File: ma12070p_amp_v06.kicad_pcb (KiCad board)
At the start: 2 copper layers, 100.4 x 80.4 mm, 83 parts, among them U1 MAX16956, U2 MA12070P

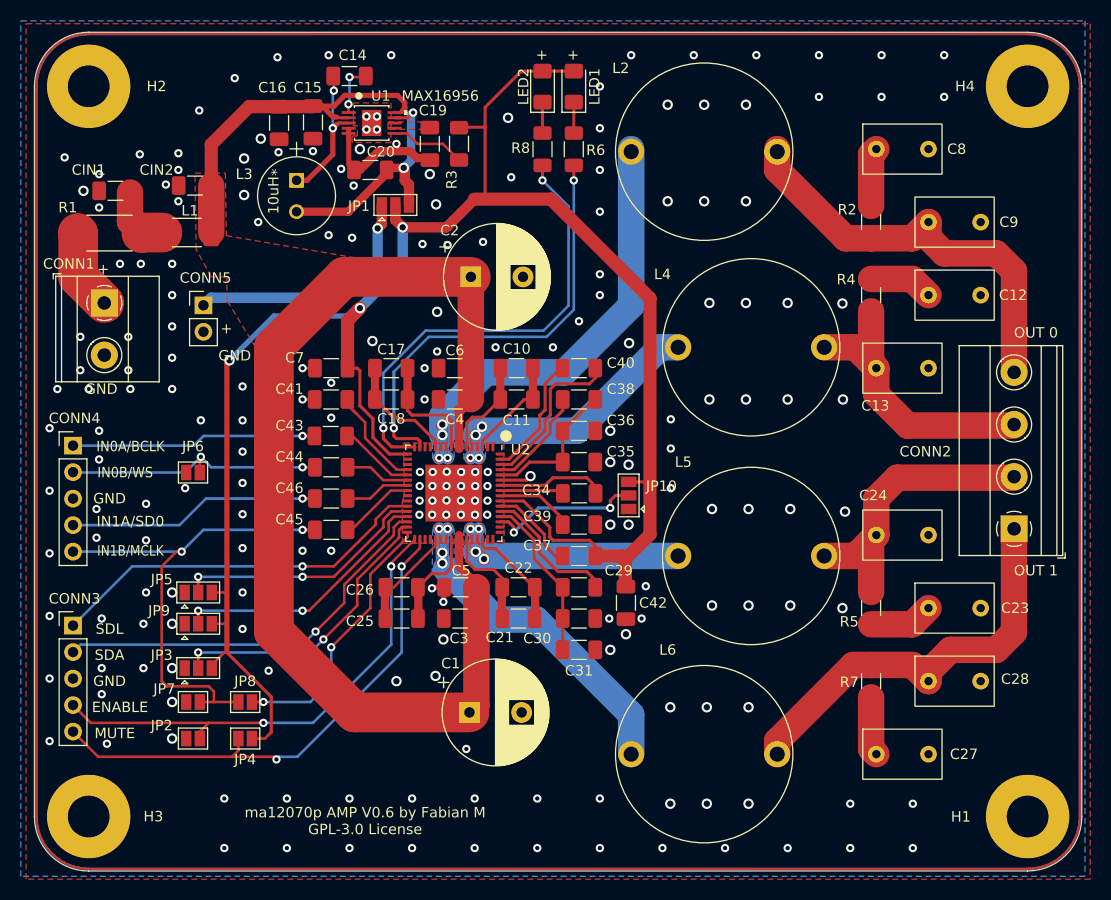
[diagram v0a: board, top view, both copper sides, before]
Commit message: Fixed VDD traces
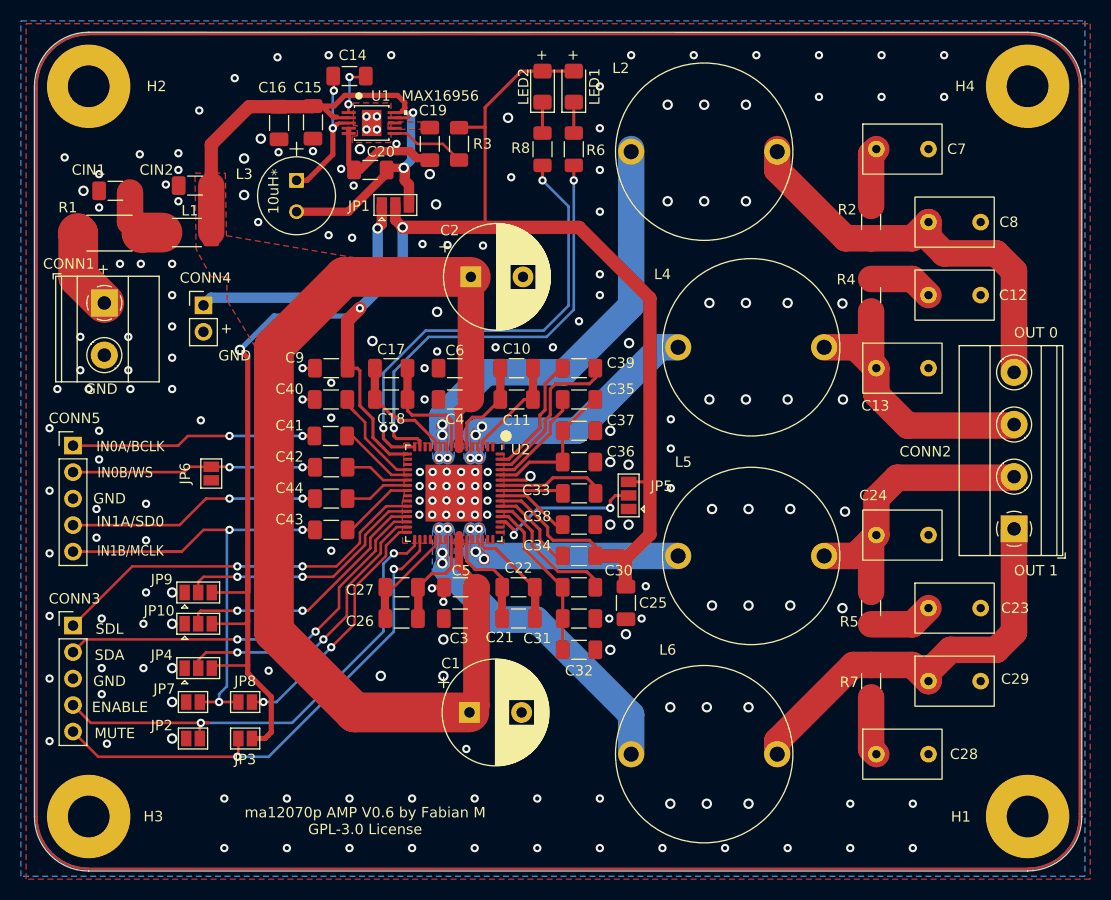
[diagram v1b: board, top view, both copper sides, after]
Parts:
- moved JP6 1.75 mm to (126.8, 86.1), turned to 90 degrees
- renumbered C42 to C25, C25 to C26, C26 to C27, C27 to C28, C28 to C29, C29 to C30, C30 to C31, C31 to C32, C34 to C33, C37 to C34, C38 to C35, C35 to C36, C36 to C37, C39 to C38, C40 to C39, C41 to C40, C43 to C41, C44 to C42, C45 to C43, C46 to C44, C8 to C7, C9 to C8, C7 to C9, CONN5 to CONN4, CONN4 to CONN5, JP9 to JP10, JP4 to JP3, JP3 to JP4, JP10 to JP5, JP5 to JP9
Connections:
- C25 pad 1: GND -> VDD
- C34 pad 1: GND -> VDD
- C9 pad 1: GND -> VDD
- JP1 pad 2: GND -> VDD
- JP10 pad 3: GND -> VDD
- JP3 pad 1: GND -> VDD
- JP4 pad 3: GND -> VDD
- JP5 pad 3: GND -> VDD
- JP9 pad 3: GND -> VDD
- LED1 pad 2: GND -> VDD
- LED2 pad 2: GND -> VDD
- R3 pad 1: GND -> VDD
- U2 pad 17: GND -> VDD
- U2 pad 55: GND -> VDD
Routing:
- net VDD: track 0.00 -> 196.4 mm, vias 0 -> 3
- net GND: track 205.6 -> 20.7 mm, vias 216 -> 203
- net Net-(C42-Pad1): track 25.7 -> 23.5 mm
- net MUTE: track 50.4 -> 48.8 mm
- net CLKIO: track 25.7 -> 24.3 mm
- net Net-(C43-Pad1): track 47.7 -> 46.6 mm, vias 2 -> 3
- net ENABLE: track 47.2 -> 47.9 mm
- net SDL: track 37.1 -> 37.4 mm, vias 1 -> 2
- net SDA: track 38.7 -> 39.0 mm, vias 1 -> 2
- net Net-(C44-Pad2): vias 1 -> 2
- net Net-(C41-Pad1): vias 1 -> 2
